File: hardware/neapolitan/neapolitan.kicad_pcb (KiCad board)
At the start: 4 copper layers, 120 x 75 mm, 280 parts, among them J1 USB-MICRO-B, J10 GND_CLIP, J11 BARREL_JACK, J2 RF-SHIELD-FRAME, J3 RF-SHIELD-COVER, J4 MOUNTING_HOLE, J5 MOUNTING_HOLE, J6 MOUNTING_HOLE, J7 MOUNTING_HOLE, J8 MOUNTING_HOLE, J9 MOUNTING_HOLE, P1 !IO_INT, P13 GPO1, P14 XCVR_CLKOUT, P15 INTR, P17 GPO6, P18 OEB, P19 GPO3, P2 !IO_RESET, P20 GPIO, P21 REF_IN, P22 I2S, P27 MIXER_SDATA, P28 SD, P31 MIXER_SCLK, P32 MIXER_ENX, P33 MIXER_RESETX, P34 MIX_BYPASS, P35 !MIX_BYPASS, P36 VAA, P39 SSP0_SCK, P4 ANTENNA, P40 SSP0_MOSI, P41 SSP0_MISO, P42 TX, P43 RX, P44 HP, P45 LP, P46 TX_MIX_BP, P47 RX_MIX_BP, P48 TX_AMP, P49 RX_AMP, P5 LEDS, P50 AMP_BYPASS, P51 !TX_AMP_PWR, P52 !RX_AMP_PWR, P53 CS_XCVR, P55 TXENABLE, P56 RXENABLE, P57 XTAL2, P6 GPO4, P67 RSSI, P7 GPO2, P80 SHIELD, P83 GND, P84 GND, P85 GND, P86 GND, P87 GND, P88 GND, P89 GND, P9 BASEBAND, P90 GND, P91 GND, P92 GND, Q1 MOSFET_P, Q2 MOSFET_P, Q3 MOSFET_P, Q4 MOSFET_P, Q5 MOSFET_P, Q6 MOSFET_P, Q7 MOSFET_P, T1 MIX_IN_BALUN, T2 MIX_OUT_BALUN, T3 RX_BALUN, T4 TX_BALUN, U1 SKY13350, U10 SKY13350, U11 SKY13350, U12 SKY13317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

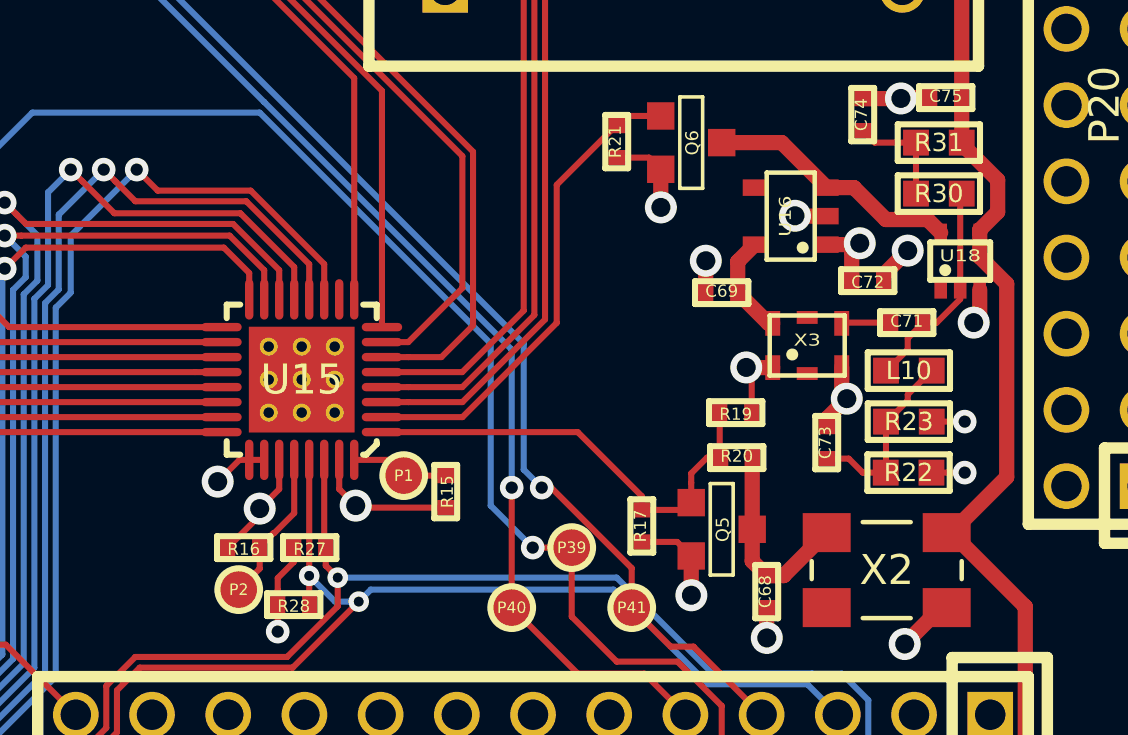
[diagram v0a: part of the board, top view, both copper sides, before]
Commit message: Neapolitan: added decoupling caps for U15 and U18
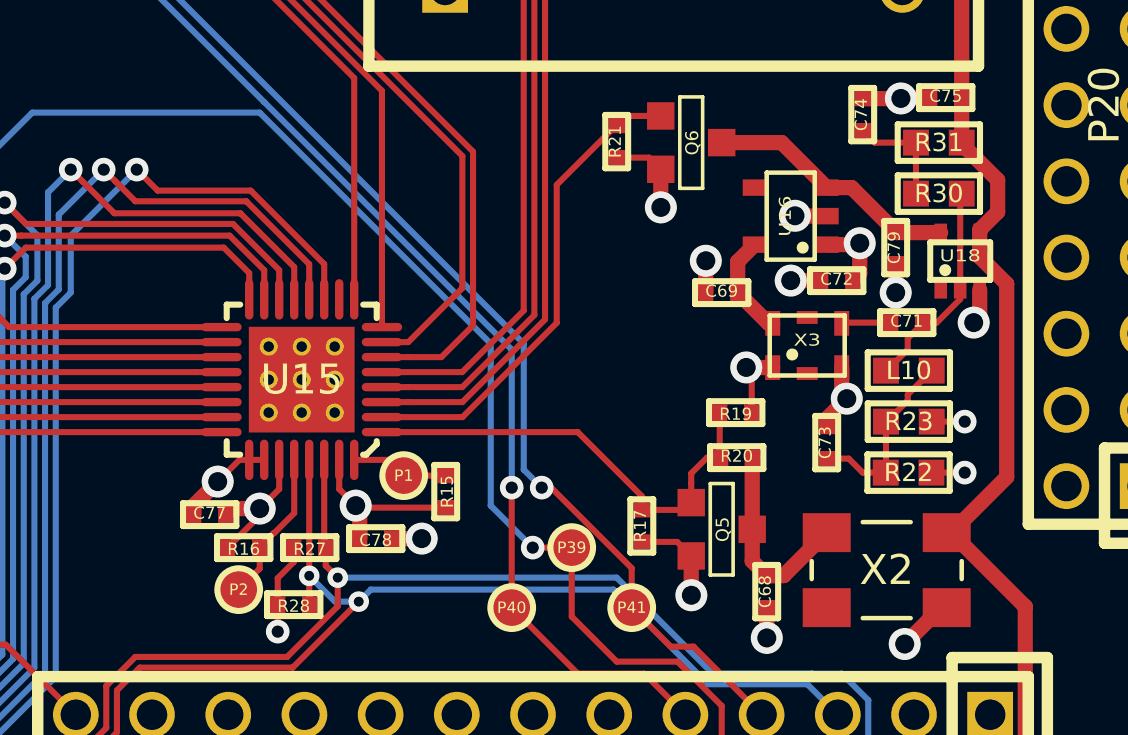
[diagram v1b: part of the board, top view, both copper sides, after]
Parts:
- added C77: 100nF, hackrf:GSG-0402, F.Cu at (141.9, 156.9)
- added C78: 100nF, hackrf:GSG-0402, F.Cu at (147.5, 157.7)
- added C79: 100nF, hackrf:GSG-0402, F.Cu at (164.8, 148.0)
- moved C72 1.03 mm to (162.8, 149.1), turned to 180 degrees
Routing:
- net GND: track 421.2 -> 424.2 mm, vias 148 -> 150
- net VCC: track 67.9 -> 70.2 mm

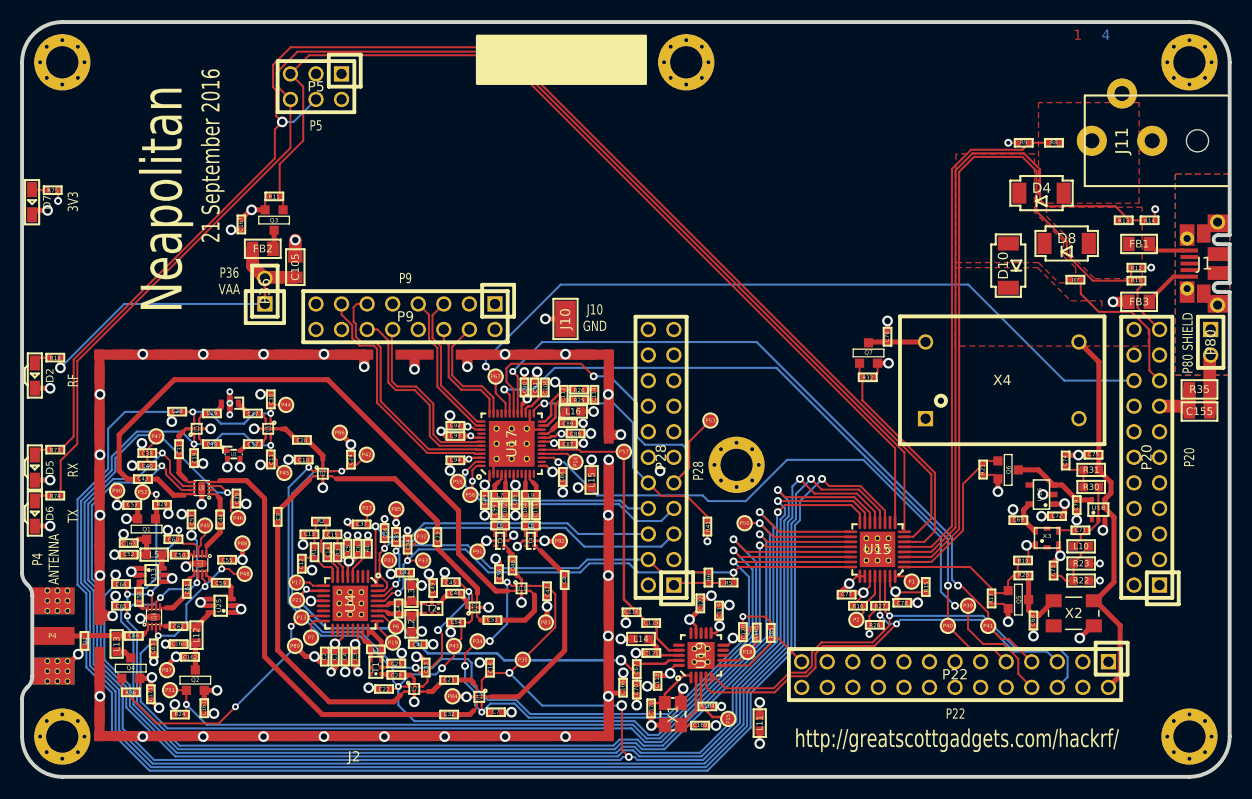
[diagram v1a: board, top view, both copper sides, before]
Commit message: Neapolitan: added decoupling caps near pin headers
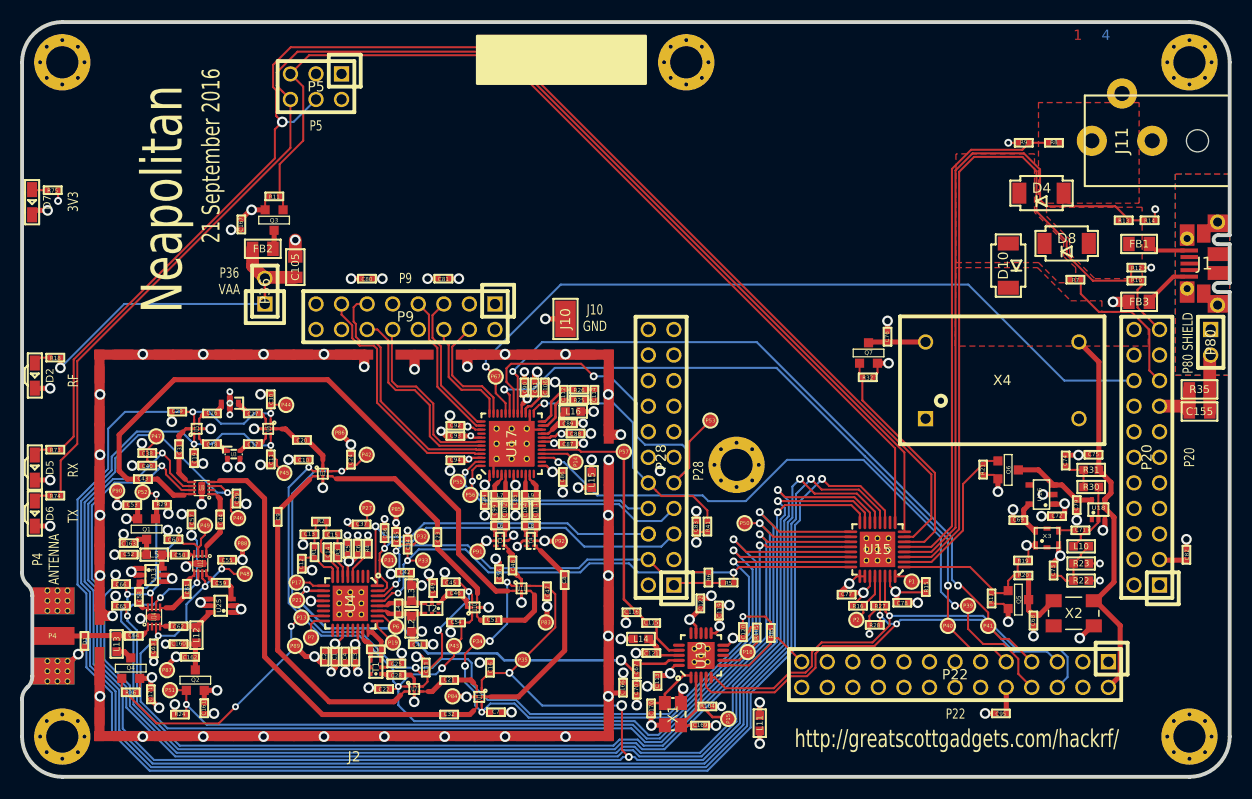
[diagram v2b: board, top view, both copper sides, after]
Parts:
- added C80: 100nF, hackrf:GSG-0402, F.Cu at (94.3, 125.5)
- added C81: 100nF, hackrf:GSG-0402, F.Cu at (101.9, 125.5)
- added C82: 100nF, hackrf:GSG-0402, F.Cu at (175.7, 152.9)
- added C83: 100nF, hackrf:GSG-0402, F.Cu at (127.0, 150.1)
- added C95: 100nF, hackrf:GSG-0402, F.Cu at (157.3, 168.7)
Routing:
- net GND: track 424.2 -> 431.0 mm, vias 150 -> 153
- net VCC: track 70.2 -> 75.0 mm, vias 19 -> 21
- net VAA: track 67.3 -> 69.4 mm, vias 20 -> 22

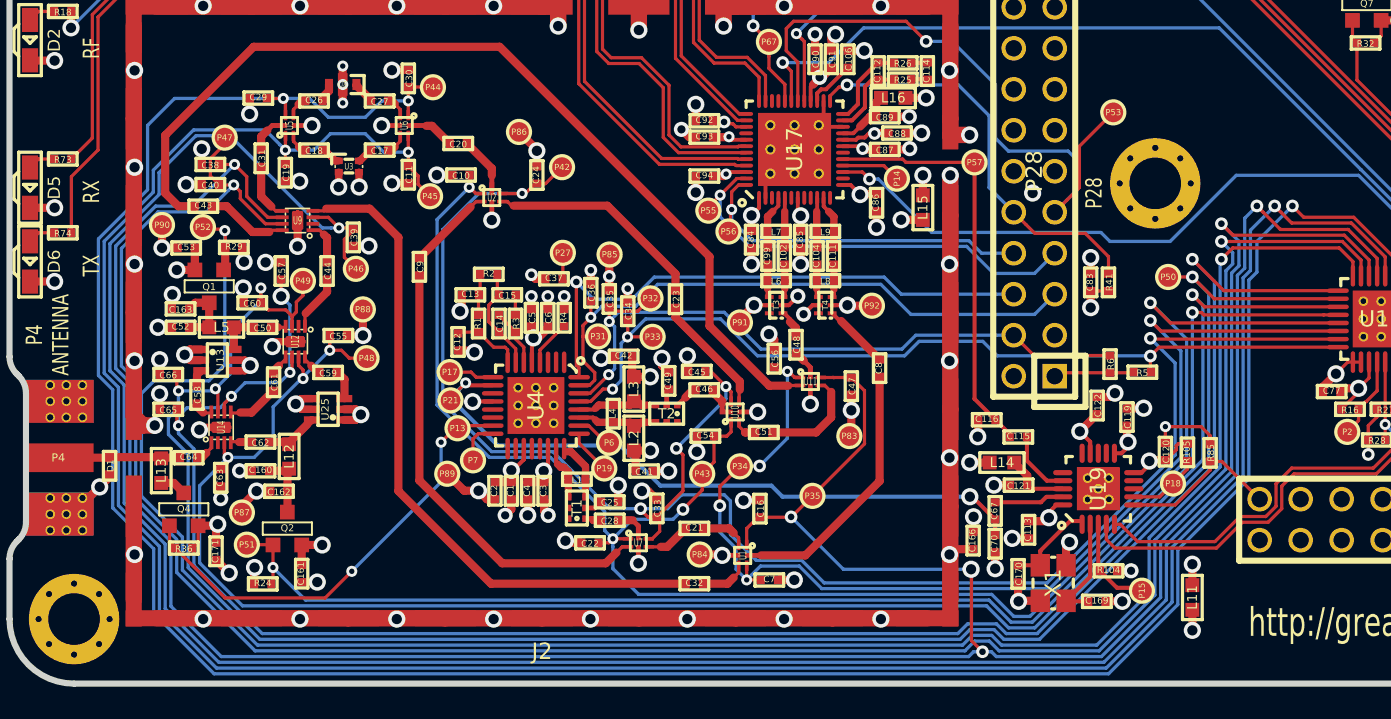
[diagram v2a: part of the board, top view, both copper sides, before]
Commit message: Neapolitan: replaced antenna port power MOSFET with current limited power switch
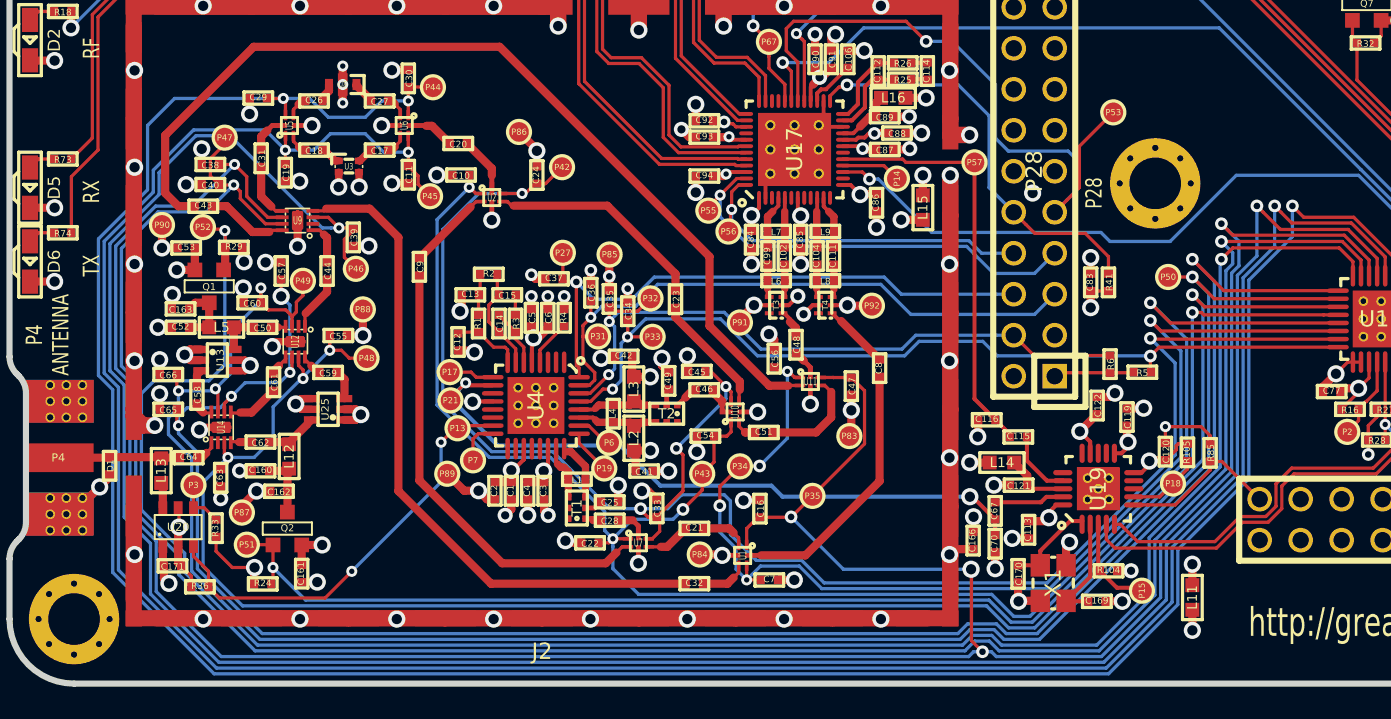
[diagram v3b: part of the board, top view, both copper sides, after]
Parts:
- removed Q4: MOSFET_P, gsg-modules:SOT23GDS
- added P3: ANT_FAULT, hackrf:GSG-TESTPOINT-50MIL, F.Cu at (71.4, 162.7)
- added R33: 10k, hackrf:GSG-0402, F.Cu at (72.8, 165.4)
- added U20: AP2553W6-7, gsg-modules:SOT457, F.Cu at (70.5, 165.3)
- moved C171 2.85 mm to (70.1, 167.7), turned to 0 degrees
- moved R36 2.60 mm to (71.8, 169.0), turned to 180 degrees
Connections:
- net /frontend/!ANT_BIAS renamed /frontend/ANT_BIAS
- R36 pad 2: VAA -> GND
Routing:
- net GND: track 431.0 -> 435.1 mm
- net Net-(P3-Pad1): track 0.00 -> 3.10 mm
- net VAA: track 69.4 -> 71.6 mm
- net /frontend/ANT_BIAS: track 28.4 -> 26.7 mm
